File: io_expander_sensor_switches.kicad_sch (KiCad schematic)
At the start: 12 parts, among them U301 PCA9535PW, U302 PCA9535PW, U303 PCA9535PW, U304 PCA9535PW

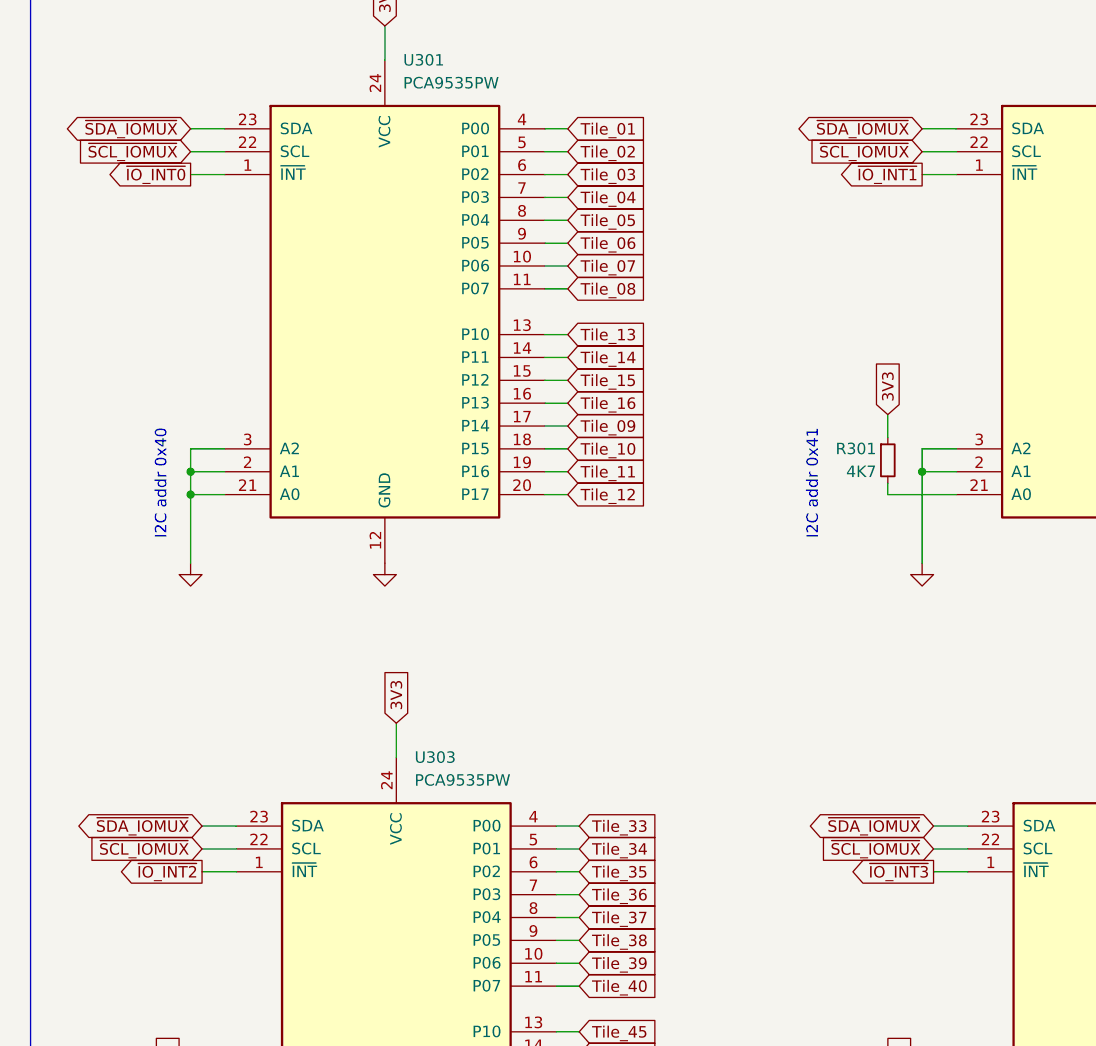
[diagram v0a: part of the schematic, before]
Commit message: fix issues in rev.b design
- fix connector design to fix potential crosstalk issues with LED data line causing unintentional LED light in the first LED in the array.
- combined all interrupts into single interrupt.
- add ground between each connector pin (to rid crosstalk).
- added in-line resistor to minimize crosstalk (33 ohms)
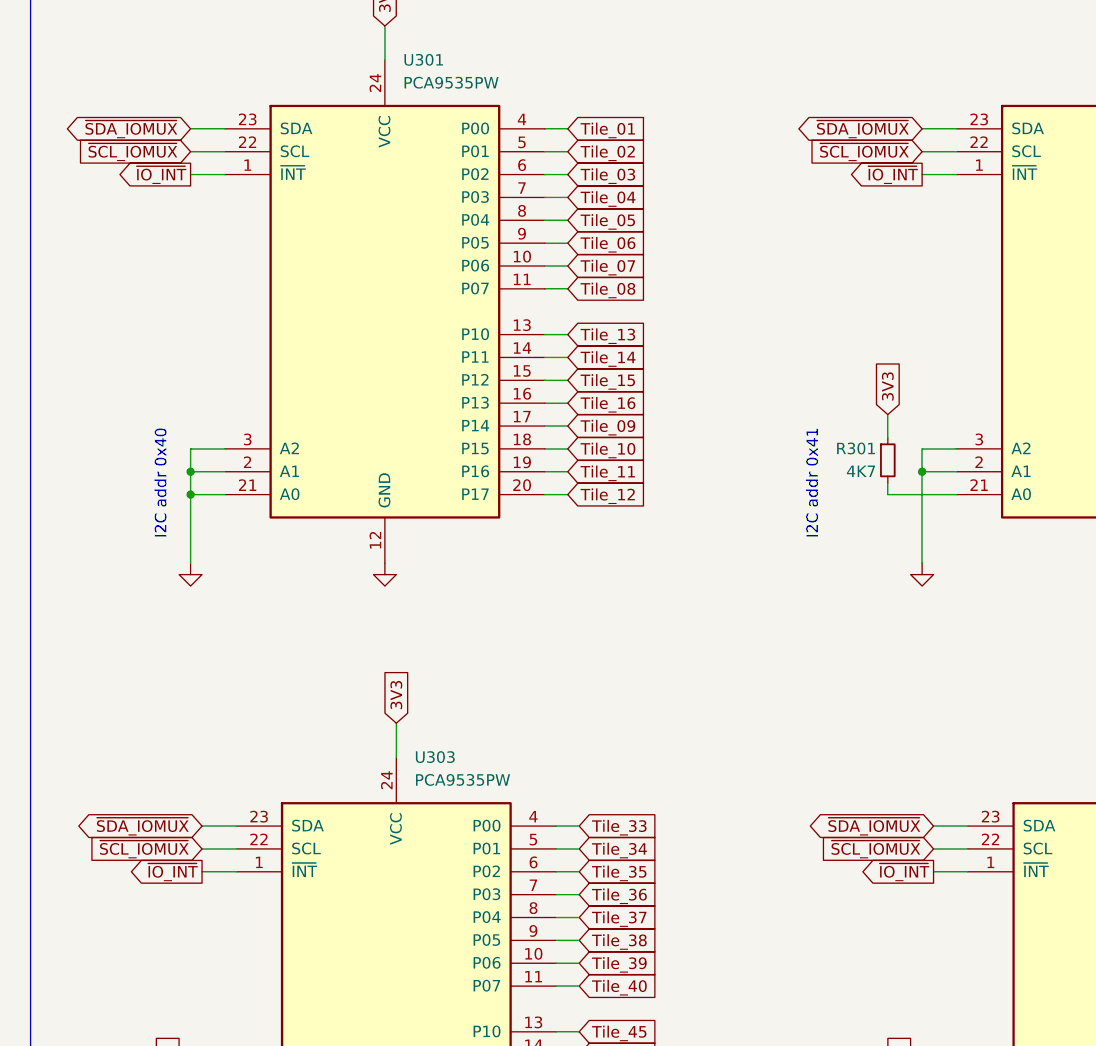
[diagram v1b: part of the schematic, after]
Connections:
- net ~{IO_INT1} is gone; now on net ~{IO_INT}: U302.1 (~{INT})
- net ~{IO_INT2} is gone; now on net ~{IO_INT}: U303.1 (~{INT})
- net ~{IO_INT3} is gone; now on net ~{IO_INT}: U304.1 (~{INT})
- net ~{IO_INT0} renamed ~{IO_INT}
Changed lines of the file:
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@@
     )
   )
-  (global_label "~{IO_INT0}" (shape output) (at 34.29 39.37 180) (fields_autoplaced)
-    (effects (font (size 1.27 1.27)) (justify right))
-    (property "Intersheet References" "${INTERSHEET_REFS}" (id 0) (at 24.8617 39.2906 0)
+  (global_label "~{IO_INT}" (shape output) (at 34.29 39.37 180) (fields_autoplaced)
+    (effects (font (size 1.27 1.27)) (justify right))
+    (property "Intersheet References" "${INTERSHEET_REFS}" (id 0) (at 26.0712 39.2906 0)
       (effects (font (size 1.27 1.27)) (justify right) hide)
     )
@@
     )
   )
-  (global_label "~{IO_INT2}" (shape output) (at 35.56 116.84 180) (fields_autoplaced)
-    (effects (font (size 1.27 1.27)) (justify right))
-    (property "Intersheet References" "${INTERSHEET_REFS}" (id 0) (at 26.1317 116.7606 0)
-      (effects (font (size 1.27 1.27)) (justify right) hide)
-    )
-  )
   (global_label "Tile_29" (shape input) (at 157.48 57.15 0) (fields_autoplaced)
     (effects (font (size 1.27 1.27)) (justify left))
@@
     )
   )
+  (global_label "~{IO_INT}" (shape output) (at 116.84 116.84 180) (fields_autoplaced)
+    (effects (font (size 1.27 1.27)) (justify right))
+    (property "Intersheet References" "${INTERSHEET_REFS}" (id 0) (at 108.6212 116.7606 0)
+      (effects (font (size 1.27 1.27)) (justify right) hide)
+    )
+  )
   (global_label "Tile_62" (shape input) (at 158.75 137.16 0) (fields_autoplaced)
     (effects (font (size 1.27 1.27)) (justify left))
@@
     )
   )
+  (global_label "~{IO_INT}" (shape output) (at 35.56 116.84 180) (fields_autoplaced)
+    (effects (font (size 1.27 1.27)) (justify right))
+    (property "Intersheet References" "${INTERSHEET_REFS}" (id 0) (at 27.3412 116.7606 0)
+      (effects (font (size 1.27 1.27)) (justify right) hide)
+    )
+  )
   (global_label "Tile_51" (shape input) (at 158.75 116.84 0) (fields_autoplaced)
     (effects (font (size 1.27 1.27)) (justify left))
@@
     )
   )
+  (global_label "~{IO_INT}" (shape output) (at 115.57 39.37 180) (fields_autoplaced)
+    (effects (font (size 1.27 1.27)) (justify right))
+    (property "Intersheet References" "${INTERSHEET_REFS}" (id 0) (at 107.3512 39.2906 0)
+      (effects (font (size 1.27 1.27)) (justify right) hide)
+    )
+  )
   (global_label "Tile_49" (shape input) (at 158.75 111.76 0) (fields_autoplaced)
     (effects (font (size 1.27 1.27)) (justify left))
@@
     )
   )
-  (global_label "~{IO_INT3}" (shape output) (at 116.84 116.84 180) (fields_autoplaced)
-    (effects (font (size 1.27 1.27)) (justify right))
-    (property "Intersheet References" "${INTERSHEET_REFS}" (id 0) (at 107.4117 116.7606 0)
-      (effects (font (size 1.27 1.27)) (justify right) hide)
-    )
-  )
   (global_label "Tile_50" (shape input) (at 158.75 114.3 0) (fields_autoplaced)
     (effects (font (size 1.27 1.27)) (justify left))
@@
     )
   )
-  (global_label "~{IO_INT1}" (shape output) (at 115.57 39.37 180) (fields_autoplaced)
-    (effects (font (size 1.27 1.27)) (justify right))
-    (property "Intersheet References" "${INTERSHEET_REFS}" (id 0) (at 106.1417 39.2906 0)
-      (effects (font (size 1.27 1.27)) (justify right) hide)
-    )
-  )

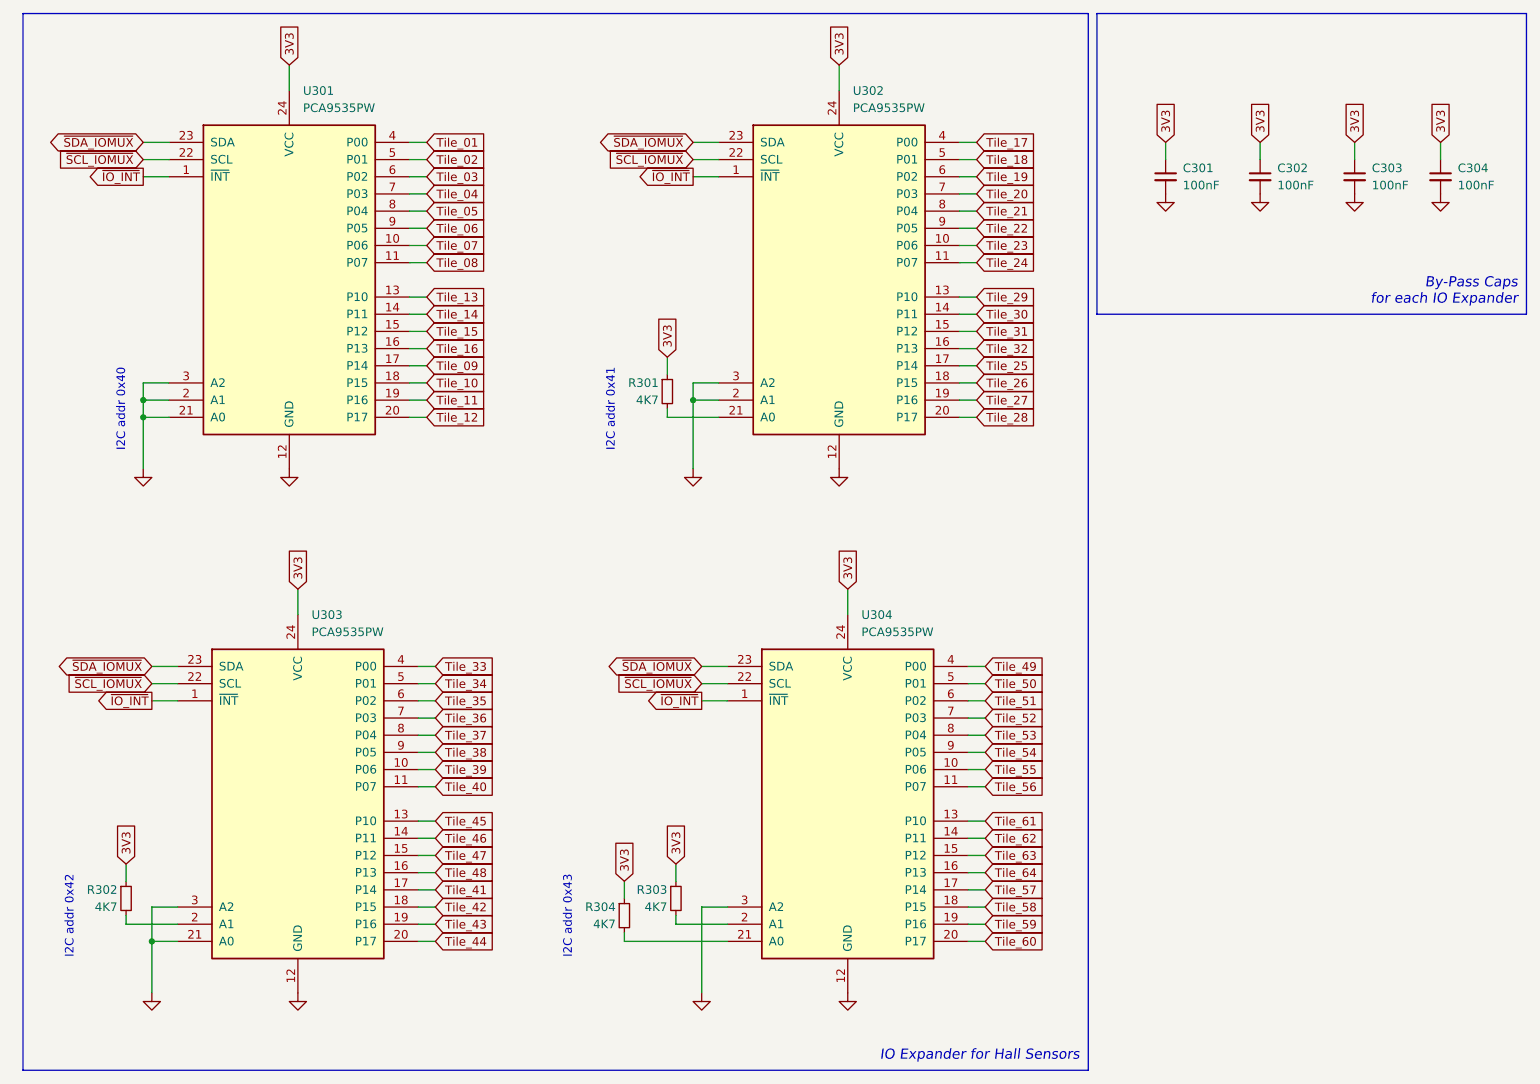
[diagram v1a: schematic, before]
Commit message: update hierarchical labels
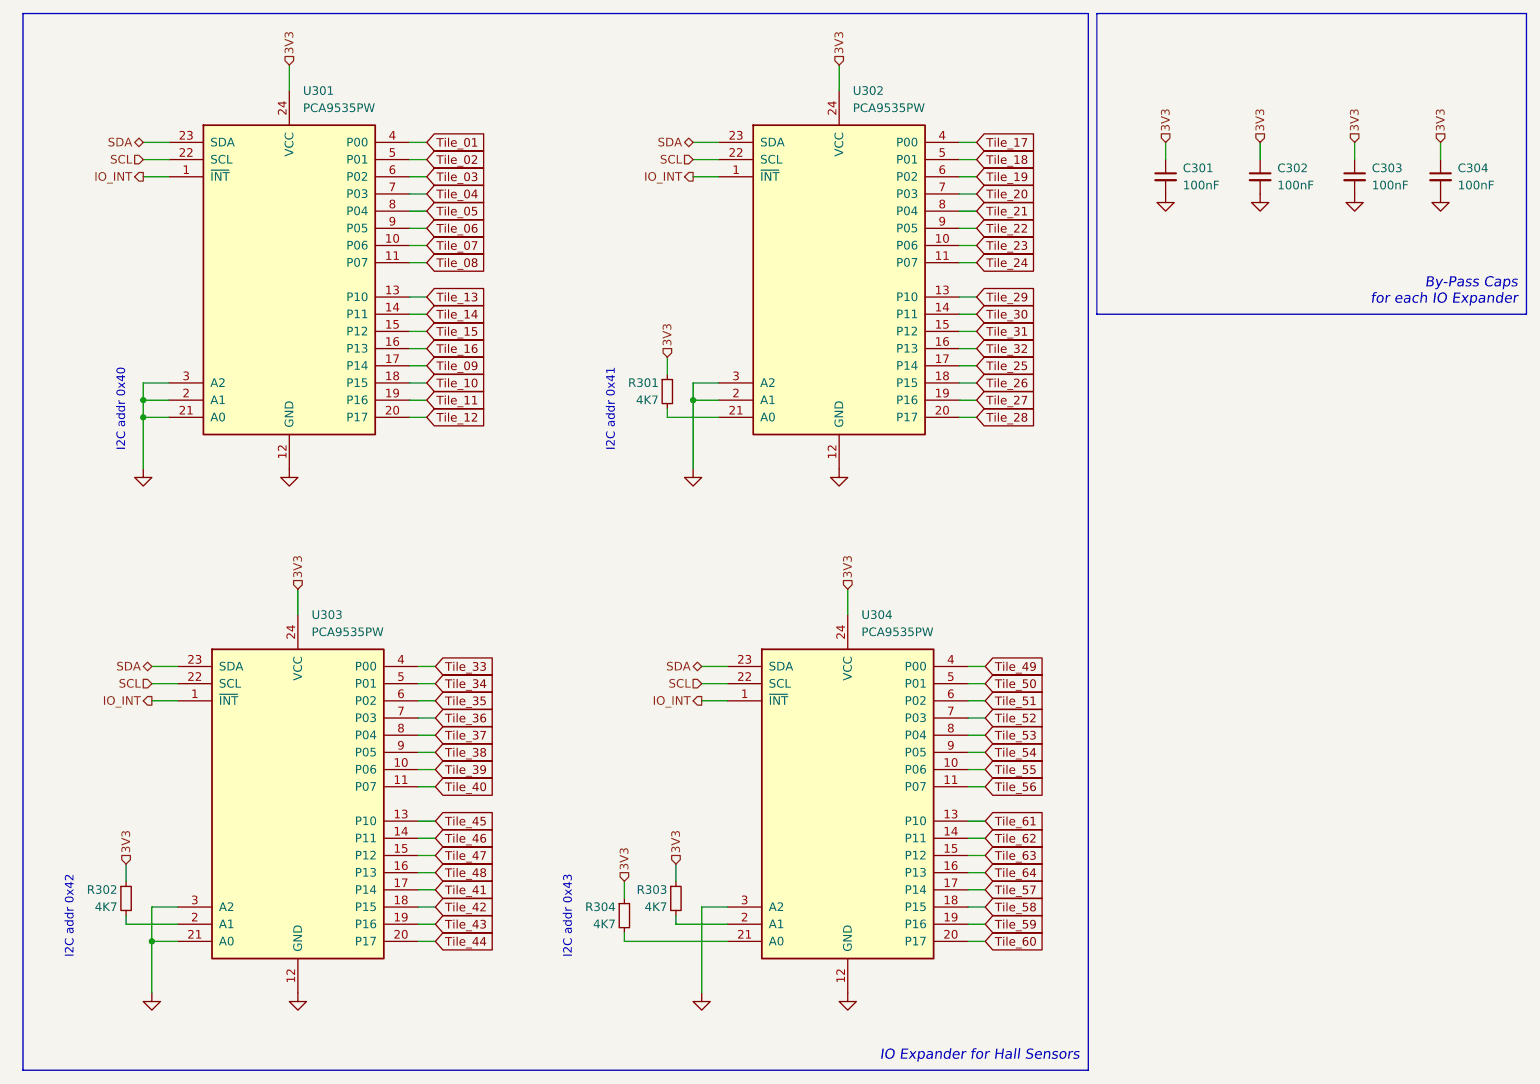
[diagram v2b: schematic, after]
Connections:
- net ~{IO_INT} renamed IO_INT
- net ~{SCL_IOMUX} renamed SCL
- net ~{SDA_IOMUX} renamed SDA
